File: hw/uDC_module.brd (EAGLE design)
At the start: 25 x 45 mm, 23 parts, among them J1 GROVE-4P-2.0-3470130P1, J2 GROVE-4P-2.0-3470130P1

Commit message: ongoing layout
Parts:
- added C10, C11: (no value), rcl:PANASONIC_D
- added C12: 33n, rcl:C0603
- added C13, C15: 100n, rcl:C0603
- added R2: 10k, rcl:R0603
- added U$7: MC33962, freescale:PQFN32
- added X1, X2: 22-23-2021, con-molex:22-23-2021
- added X3, X4: 53047-06, con-molex:53047-06
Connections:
- new net +V: C10.+, C11.+, C12.1, C13.1, U$7.P$11, U$7.P$31, U$7.P$4, U$7.P$6, X1.1
- new net MA: U$7.P$12, U$7.P$13, U$7.P$14, U$7.P$15, X2.1
- new net MB: U$7.P$27, U$7.P$28, U$7.P$29, U$7.P$30, X2.2
- new net N$10: U$7.P$7
- new net N$11: U$7.P$26
- new net N$12: U$7.P$16
- new net N$13: U$7.P$1
- new net N$14: U$7.P$2
- new net N$15: U$7.P$10
- new net N$3: C15.1, R2.2, U$7.P$8
- new net N$5: U$7.P$21
- new net N$6: C12.2, U$7.P$32
- new net N$9: U$7.P$3
- net GND: now also C10.-, C11.-, C13.2, C15.2, R2.1, U$7.P$18, U$7.P$19, U$7.P$20, U$7.P$22, U$7.P$23, U$7.P$24, U$7.P$33, U$7.P$5, X1.2
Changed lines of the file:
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@@
 <element name="U$1" library="r2p_pcb" package="25X45" value="PCB_25X45" x="0" y="0"/>
 <element name="U$5" library="abracon" package="2.5X2" value="ASD" x="22.7" y="16" rot="R180"/>
+<element name="C10" library="rcl" package="PANASONIC_D" value="" x="18.5" y="32.5"/>
+<element name="C11" library="rcl" package="PANASONIC_D" value="" x="18.5" y="25.5"/>
+<element name="X1" library="con-molex" package="22-23-2021" value="22-23-2021" x="20.4" y="40.7" rot="R180">
+<attribute name="OC_NEWARK" value="25C3832" x="27.4" y="43.2" size="1.778" layer="27" rot="R180" display="off"/>
+<attribute name="MPN" value="22-23-2021" x="27.4" y="43.2" size="1.778" layer="27" rot="R180" display="off"/>
+<attribute name="MF" value="MOLEX" x="27.4" y="43.2" size="1.778" layer="27" rot="R180" display="off"/>
+<attribute name="OC_FARNELL" value="1462926" x="27.4" y="43.2" size="1.778" layer="27" rot="R180" display="off"/>
+</element>
+<element name="X2" library="con-molex" package="22-23-2021" value="22-23-2021" x="4.6" y="40.7" rot="R180">
+<attribute name="OC_NEWARK" value="25C3832" x="26.6" y="43.2" size="1.778" layer="27" rot="R180" display="off"/>
+<attribute name="MPN" value="22-23-2021" x="26.6" y="43.2" size="1.778" layer="27" rot="R180" display="off"/>
+<attribute name="MF" value="MOLEX" x="26.6" y="43.2" size="1.778" layer="27" rot="R180" display="off"/>
+<attribute name="OC_FARNELL" value="1462926" x="26.6" y="43.2" size="1.778" layer="27" rot="R180" display="off"/>
+</element>
+<element name="X3" library="con-molex" package="53047-06" value="53047-06" x="12.5" y="42.4">
+<attribute name="OC_NEWARK" value="03M2965" x="-9.5" y="39.9" size="1.778" layer="27" display="off"/>
+<attribute name="MPN" value="53047-0610-C" x="-9.5" y="39.9" size="1.778" layer="27" display="off"/>
+<attribute name="MF" value="" x="-9.5" y="39.9" size="1.778" layer="27" display="off"/>
+<attribute name="OC_FARNELL" value="9733078" x="-9.5" y="39.9" size="1.778" layer="27" display="off"/>
+</element>
+<element name="C12" library="rcl" package="C0603" value="33n" x="-3" y="-32"/>
+<element name="U$7" library="freescale" package="PQFN32" value="MC33962" x="9.5" y="28.5" rot="R180"/>
+<element name="C13" library="rcl" package="C0603" value="100n" x="13" y="-25"/>
+<element name="C15" library="rcl" package="C0603" value="100n" x="-3" y="-37"/>
+<element name="R2" library="rcl" package="R0603" value="10k" x="-3" y="-42"/>
+<element name="X4" library="con-molex" package="53047-06" value="53047-06" x="12.5" y="39">
+<attribute name="OC_NEWARK" value="03M2965" x="12.5" y="39" size="1.778" layer="27" display="off"/>
+<attribute name="MPN" value="53047-0610-C" x="12.5" y="39" size="1.778" layer="27" display="off"/>
+<attribute name="MF" value="" x="12.5" y="39" size="1.778" layer="27" display="off"/>
+<attribute name="OC_FARNELL" value="9733078" x="12.5" y="39" size="1.778" layer="27" display="off"/>
+</element>
 </elements>
 <signals>
@@
 <contactref element="U$5" pad="2"/>
 <contactref element="U$5" pad="2"/>
+<contactref element="C10" pad="-"/>
+<contactref element="X1" pad="2"/>
+<contactref element="C13" pad="2"/>
+<contactref element="C15" pad="2"/>
+<contactref element="R2" pad="1"/>
+<contactref element="U$7" pad="P$5"/>
+<contactref element="U$7" pad="P$33"/>
+<contactref element="U$7" pad="P$19"/>
+<contactref element="U$7" pad="P$23"/>
+<contactref element="U$7" pad="P$18"/>
+<contactref element="U$7" pad="P$22"/>
+<contactref element="U$7" pad="P$20"/>
+<contactref element="U$7" pad="P$24"/>
+<contactref element="C11" pad="-"/>
+<wire x1="-2.15" y1="-37" x2="-3.85" y2="-42" width="0" layer="19" extent="1-1"/>
+<wire x1="13.85" y1="-25" x2="-2.15" y2="-37" width="0" layer="19" extent="1-1"/>
+<wire x1="23.4" y1="0.9" x2="13.85" y2="-25" width="0" layer="19" extent="1-1"/>
 </signal>
 <signal name="VIN">
@@
 <signal name="N$2">
 </signal>
+<signal name="N$6">
+<contactref element="C12" pad="2"/>
+<contactref element="U$7" pad="P$32"/>
+<wire x1="7.1" y1="24.9" x2="-2.15" y2="-32" width="0" layer="19" extent="1-1"/>
+</signal>
+<signal name="+V">
+<contactref element="C12" pad="1"/>
+<contactref element="U$7" pad="P$11"/>
+<contactref element="U$7" pad="P$6"/>
+<contactref element="U$7" pad="P$31"/>
+<contactref element="U$7" pad="P$4"/>
+<contactref element="X1" pad="1"/>
+<contactref element="C13" pad="1"/>
+<contactref element="C10" pad="+"/>
+<contactref element="C11" pad="+"/>
+<wire x1="20.9" y1="32.5" x2="21.67" y2="40.7" width="0" layer="19" extent="1-1"/>
+<wire x1="20.9" y1="25.5" x2="20.9" y2="32.5" width="0" layer="19" extent="1-1"/>
+<wire x1="7.9" y1="32.1" x2="20.9" y2="32.5" width="0" layer="19" extent="1-1"/>
+<wire x1="5.9" y1="29.3" x2="7.9" y2="32.1" width="0" layer="19" extent="1-1"/>
+<wire x1="5.9" y1="27.7" x2="5.9" y2="29.3" width="0" layer="19" extent="1-1"/>
+<wire x1="7.9" y1="24.9" x2="5.9" y2="27.7" width="0" layer="19" extent="1-1"/>
+<wire x1="12.15" y1="-25" x2="7.9" y2="24.9" width="0" layer="19" extent="1-1"/>
+<wire x1="-3.85" y1="-32" x2="12.15" y2="-25" width="0" layer="19" extent="1-1"/>
+</signal>
+<signal name="MA">
+<contactref element="U$7" pad="P$15"/>
+<contactref element="U$7" pad="P$14"/>
+<contactref element="U$7" pad="P$13"/>
+<contactref element="U$7" pad="P$12"/>
+<contactref element="X2" pad="1"/>
+<wire x1="8.7" y1="32.1" x2="5.87" y2="40.7" width="0" layer="19" extent="1-1"/>
+<wire x1="9.5" y1="32.1" x2="8.7" y2="32.1" width="0" layer="19" extent="1-1"/>
+<wire x1="10.3" y1="32.1" x2="9.5" y2="32.1" width="0" layer="19" extent="1-1"/>
+<wire x1="11.1" y1="32.1" x2="10.3" y2="32.1" width="0" layer="19" extent="1-1"/>
+</signal>
+<signal name="MB">
+<contactref element="U$7" pad="P$28"/>
+<contactref element="U$7" pad="P$27"/>
+<contactref element="U$7" pad="P$30"/>
+<contactref element="U$7" pad="P$29"/>
+<contactref element="X2" pad="2"/>
+<wire x1="8.7" y1="24.9" x2="3.33" y2="40.7" width="0" layer="19" extent="1-1"/>
+<wire x1="9.5" y1="24.9" x2="8.7" y2="24.9" width="0" layer="19" extent="1-1"/>
+<wire x1="10.3" y1="24.9" x2="9.5" y2="24.9" width="0" layer="19" extent="1-1"/>
+<wire x1="11.1" y1="24.9" x2="10.3" y2="24.9" width="0" layer="19" extent="1-1"/>
+</signal>
+<signal name="N$3">
+<contactref element="U$7" pad="P$8"/>
+<contactref element="C15" pad="1"/>
+<contactref element="R2" pad="2"/>
+<wire x1="-3.85" y1="-37" x2="-2.15" y2="-42" width="0" layer="19" extent="1-1"/>
+<wire x1="5.9" y1="30.9" x2="-3.85" y2="-37" width="0" layer="19" extent="1-1"/>
+</signal>
+<signal name="N$5">
+<contactref element="U$7" pad="P$21"/>
+</signal>
+<signal name="N$9">
+<contactref element="U$7" pad="P$3"/>
+</signal>
+<signal name="N$10">
+<contactref element="U$7" pad="P$7"/>
+</signal>
+<signal name="N$11">
+<contactref element="U$7" pad="P$26"/>
+</signal>
+<signal name="N$12">
+<contactref element="U$7" pad="P$16"/>
+</signal>
+<signal name="N$13">
+<contactref element="U$7" pad="P$1"/>
+</signal>
+<signal name="N$14">
+<contactref element="U$7" pad="P$2"/>
+</signal>
+<signal name="N$15">
+<contactref element="U$7" pad="P$10"/>
+</signal>
 </signals>

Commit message: ongoing layout
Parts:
- U$6: value STM32F103CX -> STM32F103CXTX
- moved R2 67.7 mm to (14.1, 23.5), turned to 90 degrees
- moved C15 62.5 mm to (12.6, 23.5), turned to 270 degrees
- moved C12 58.3 mm to (2.70, 26.0)
- moved C13 48.3 mm to (8.80, 23.1), turned to 270 degrees
- moved X1 10.00 mm to (10.4, 40.7)
- moved X3 6.00 mm to (18.5, 42.4)
- moved X4 6.00 mm to (18.5, 39.0)
- moved U$7 2.02 mm to (8.80, 30.4), turned to 90 degrees
- moved C10 0.71 mm to (19.0, 32.0)
- moved C11 0.58 mm to (19.0, 25.2)
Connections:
- net N$10 renamed INV
- net N$11 renamed D1
- net N$12 renamed !D2
- net N$13 renamed IN2
- net N$14 renamed IN1
- net N$15 renamed EN
- net N$3 renamed FB
- net N$5 renamed !SF
- net N$9 renamed SLEW
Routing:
- net !SF: track 0.00 -> 0.90 mm, vias 0 -> 1
- added copper zone on layer 16, net +V
- added copper zone on layer 1, net MA
- added copper zone on layer 1, net MB

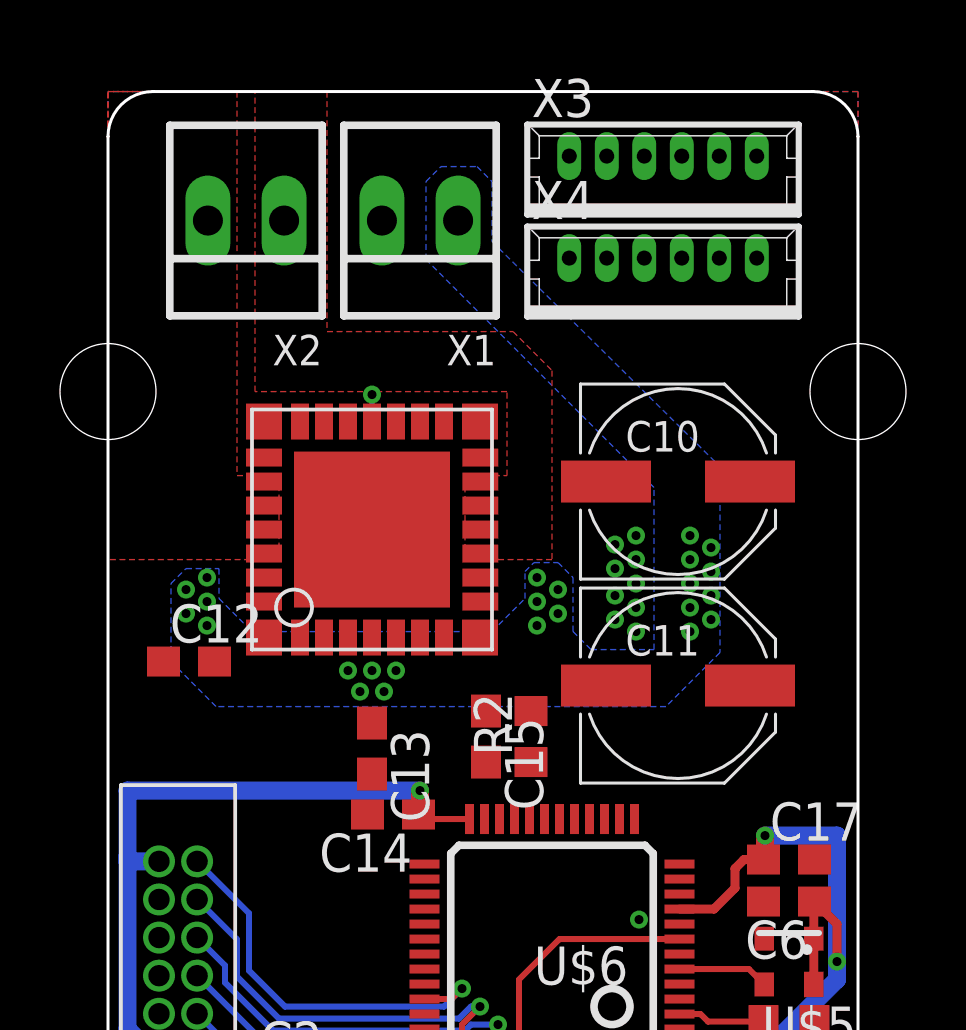
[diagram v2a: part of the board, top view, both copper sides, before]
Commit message: hi-power section layout completed
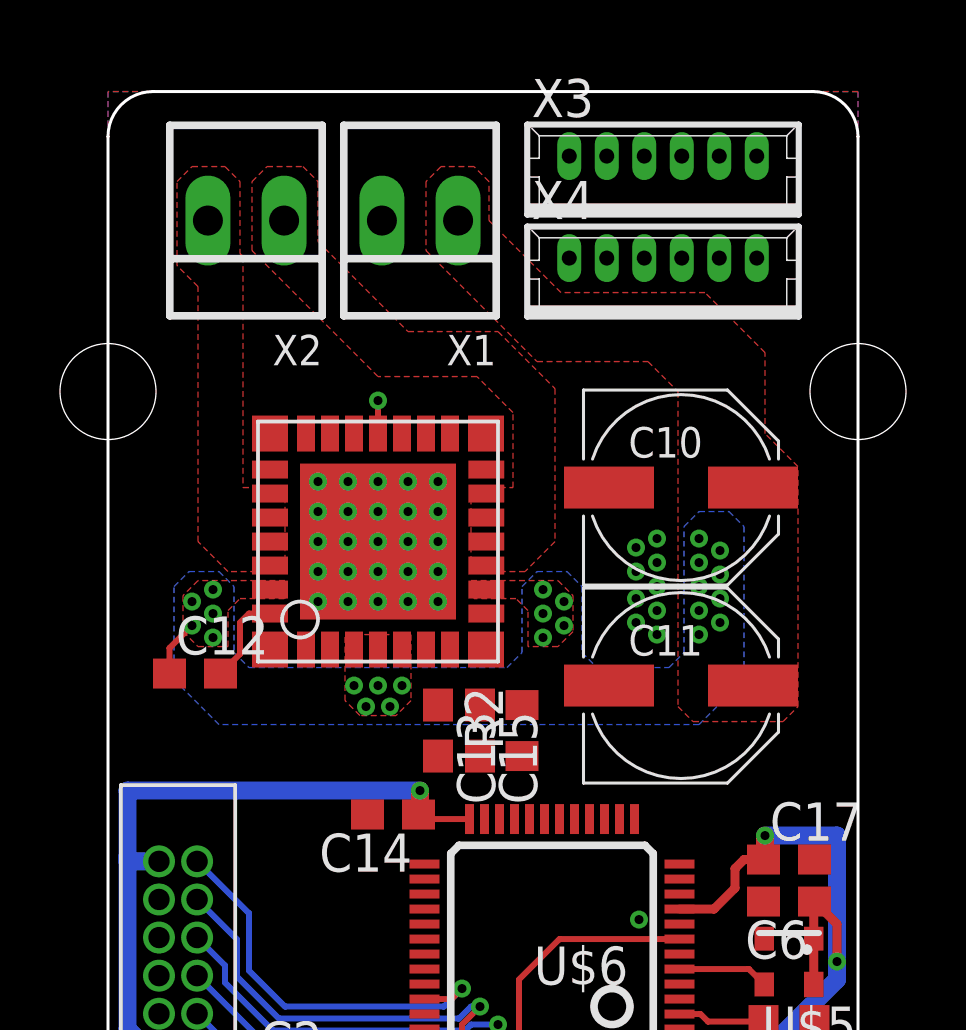
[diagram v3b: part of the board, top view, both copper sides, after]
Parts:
- moved C13 2.28 mm to (11.0, 23.7)
- moved C12 0.45 mm to (2.90, 25.6)
- moved U$7 0.45 mm to (9.00, 30.0)
- moved R2 0.36 mm to (13.8, 23.7)
- moved C15 0.28 mm to (12.4, 23.7)
- moved C10 0.22 mm to (19.1, 31.8)
- moved C11 0.10 mm to (19.1, 25.2)
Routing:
- net N$6: track 0.00 -> 3.09 mm
- net +V: track 0.00 -> 1.91 mm
- added copper zone on layer 1, net +V

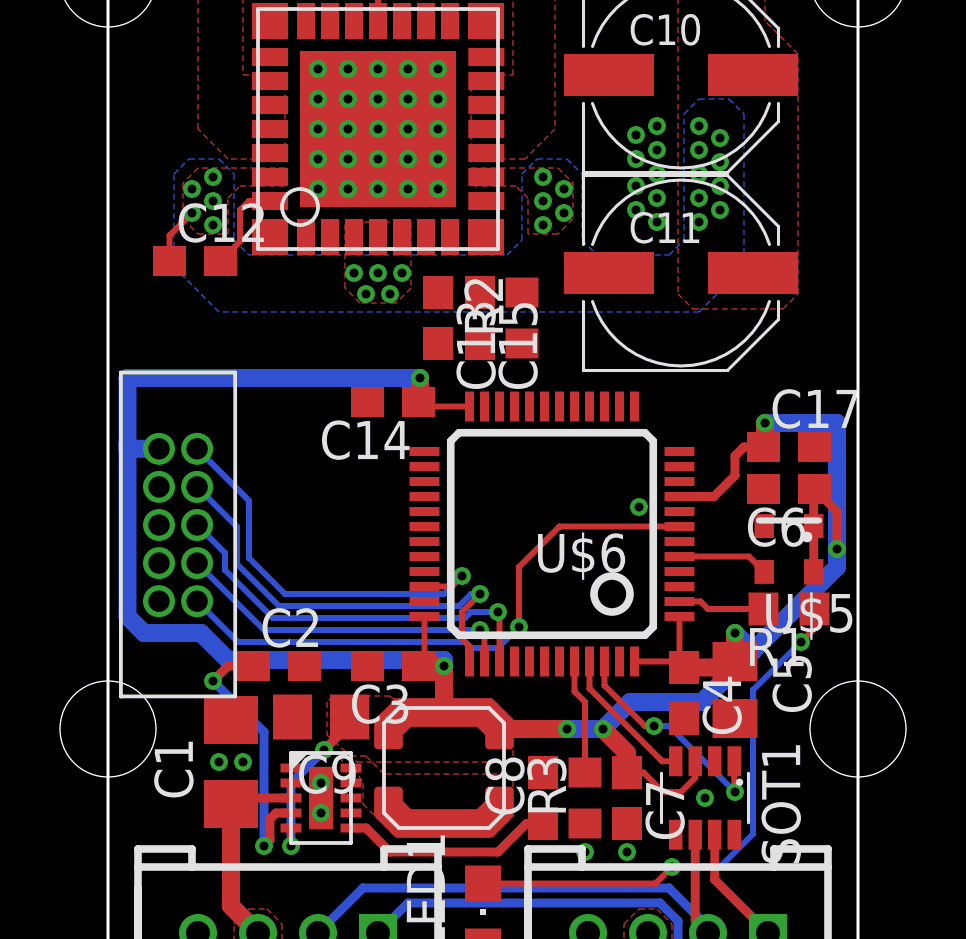
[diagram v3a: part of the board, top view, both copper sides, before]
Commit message: working on signal routing
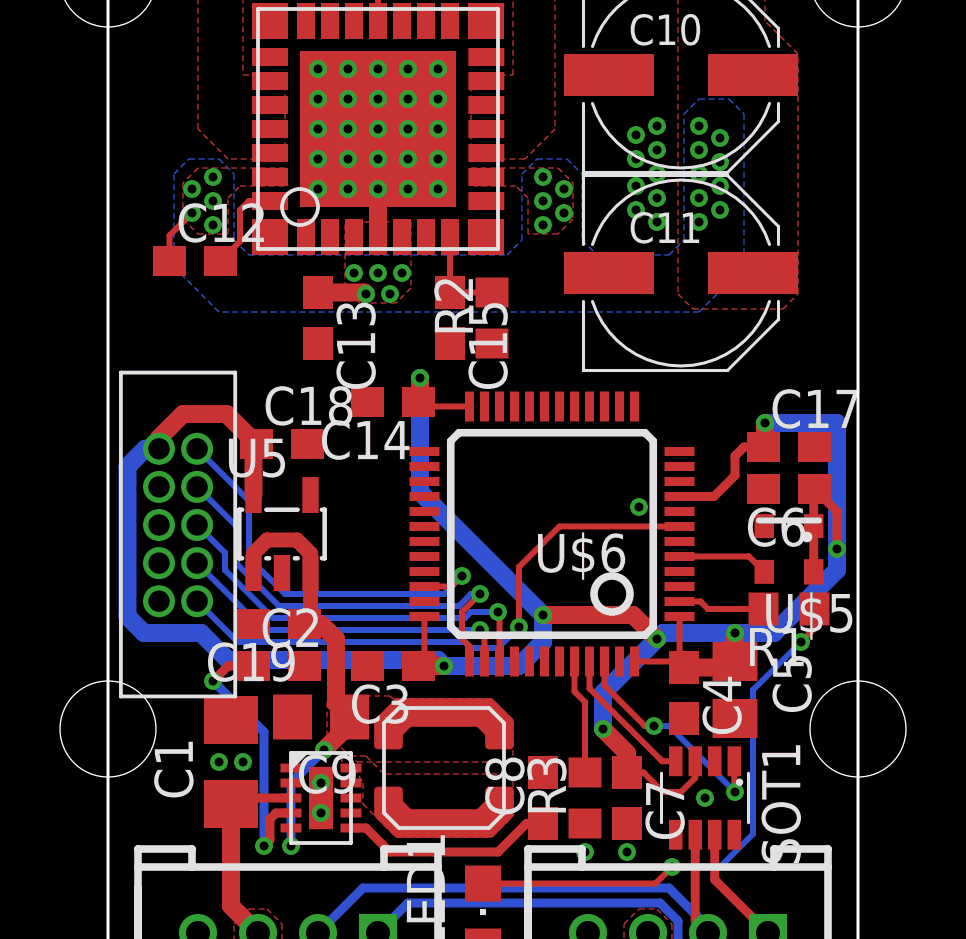
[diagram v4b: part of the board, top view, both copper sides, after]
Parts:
- added C18, C19: 1u, rcl:C0603
- added U5: LD3985XX, st:SOT23-5L
- moved C13 4.00 mm to (7.00, 23.7)
- moved C15 1.00 mm to (11.4, 23.7)
- moved R2 1.00 mm to (12.8, 23.7)
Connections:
- new net +5V: C19.1, C9.1, U$2.P$2, U$3.P$5, U5.1, U5.3
- net +3V3: now also C18.1, U5.5; no longer C9.1, U$2.P$2, U$3.P$5
- net GND: now also C18.2, C19.2, U5.2
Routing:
- net +5V: track 0.00 -> 15.1 mm, vias 0 -> 2
- net FB: track 0.00 -> 3.25 mm
- net +V: track 1.91 -> 3.53 mm
- net GND: track 0.00 -> 1.60 mm
- net +3V3: track 86.0 -> 86.5 mm, vias 9 -> 8
- added copper zone on layer 1, net +5V
- removed copper zone on layer 1, net +3V3
